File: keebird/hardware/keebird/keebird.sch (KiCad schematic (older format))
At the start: 9 parts

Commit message: Wire in 1.69 OLED display to the schematic.
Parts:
- added C?: 470uf, symbol Device:C_Small
- added J?: NHD_OLED_Display_Connector, symbol Connector:Conn_01x20_Male
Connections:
- net +3V3: now also C?.1, C?.2, J?.1 (Pin_1), J?.15 (Pin_15), J?.18 (Pin_18), J?.19 (Pin_19), J?.2 (Pin_2), J?.20 (Pin_20)
- net ADDR_0: now also J?.4 (Pin_4)
- net DATA_0: now also J?.7 (Pin_7)
- net DATA_1: now also J?.8 (Pin_8)
- net DATA_2: now also J?.9 (Pin_9)
- net DATA_3: now also J?.10 (Pin_10)
- net DATA_4: now also J?.11 (Pin_11)
- net DATA_5: now also J?.12 (Pin_12)
- net DATA_6: now also J?.13 (Pin_13)
- net DATA_7: now also J?.14 (Pin_14)
- net ~LCD_RST: now reaches U?.116 (PD2)
- net ~LCD_RST: now also J?.16 (Pin_16)
- net MEM_RD: now reaches U?.118 (PD4)
- net MEM_RD: now also J?.6 (Pin_6)
- net MEM_WR: now reaches U?.119 (PD5)
- net MEM_WR: now also J?.5 (Pin_5)
- net LCD_CS: now reaches U?.123 (PD7)
- net LCD_CS: now also J?.17 (Pin_17)
- no-connect marks 0 -> 1
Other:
- note added: "Place near LCD Power Pins"
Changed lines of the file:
@@
 LIBS:contrib
 LIBS:valves
+LIBS:keebird-cache
 EELAYER 26 0
 EELAYER END
@@
 Text Notes 9700 850  0    50   ~ 0
 Place Near RAM\n
+$Comp
+L Connector:Conn_01x20_Male J?
+U 1 1 5B82E830
+P 12050 6350
+F 0 "J?" H 12156 7428 50  0000 C CNN
+F 1 "NHD_OLED_Display_Connector" H 12156 7337 50  0000 C CNN
+F 2 "" H 12050 6350 50  0001 C CNN
+F 3 "~" H 12050 6350 50  0001 C CNN
+	1    12050 6350
+	1    0    0    -1
+$EndComp
+NoConn ~ 12250 5650
+Wire Wire Line
+	12250 6050 12450 6050
+Text Label 12450 6050 0    50   ~ 0
+DATA_0
+Wire Wire Line
+	12250 6150 12450 6150
+Text Label 12450 6150 0    50   ~ 0
+DATA_1
+Wire Wire Line
+	12250 6250 12450 6250
+Text Label 12450 6250 0    50   ~ 0
+DATA_2
+Wire Wire Line
+	12250 6350 12450 6350
+Text Label 12450 6350 0    50   ~ 0
+DATA_3
+Wire Wire Line
+	12250 6450 12450 6450
+Text Label 12450 6450 0    50   ~ 0
+DATA_4
+Wire Wire Line
+	12250 6550 12450 6550
+Text Label 12450 6550 0    50   ~ 0
+DATA_5
+Wire Wire Line
+	12250 6650 12450 6650
+Text Label 12450 6650 0    50   ~ 0
+DATA_6
+Wire Wire Line
+	12250 6750 12450 6750
+Text Label 12450 6750 0    50   ~ 0
+DATA_7
+Wire Wire Line
+	8250 7450 8500 7450
+Text Label 8500 7450 0    50   ~ 0
+LCD_CS
+Wire Wire Line
+	12250 7050 12450 7050
+Text Label 12450 7050 0    50   ~ 0
+LCD_CS
+Wire Wire Line
+	8250 7150 8500 7150
+Text Label 8500 7150 0    50   ~ 0
+MEM_RD
+Wire Wire Line
+	12250 5950 12450 5950
+Text Label 12450 5950 0    50   ~ 0
+MEM_RD
+Wire Wire Line
+	8250 7250 8500 7250
+Text Label 8500 7250 0    50   ~ 0
+MEM_WR
+Wire Wire Line
+	12250 5850 12450 5850
+Text Label 12450 5850 0    50   ~ 0
+MEM_WR
+Wire Wire Line
+	12250 5750 12450 5750
+Text Label 12450 5750 0    50   ~ 0
+ADDR_0
+Wire Wire Line
+	12250 6850 12450 6850
+$Comp
+L power:GND #PWR?
+U 1 1 5B8D1D5F
+P 12450 6850
+F 0 "#PWR?" H 12450 6600 50  0001 C CNN
+F 1 "GND" V 12455 6722 50  0000 R CNN
+F 2 "" H 12450 6850 50  0001 C CNN
+F 3 "" H 12450 6850 50  0001 C CNN
+	1    12450 6850
+	0    -1   -1   0
+$EndComp
+Wire Wire Line
+	12250 7150 12450 7150
+$Comp
+L power:GND #PWR?
+U 1 1 5B8DAB90
+P 12450 7150
+F 0 "#PWR?" H 12450 6900 50  0001 C CNN
+F 1 "GND" V 12455 7022 50  0000 R CNN
+F 2 "" H 12450 7150 50  0001 C CNN
+F 3 "" H 12450 7150 50  0001 C CNN
+	1    12450 7150
+	0    -1   -1   0
+$EndComp
+Wire Wire Line
+	12250 7350 12450 7350
+$Comp
+L power:GND #PWR?
+U 1 1 5B8E3ACA
+P 12450 7350
+F 0 "#PWR?" H 12450 7100 50  0001 C CNN
+F 1 "GND" V 12455 7222 50  0000 R CNN
+F 2 "" H 12450 7350 50  0001 C CNN
+F 3 "" H 12450 7350 50  0001 C CNN
+	1    12450 7350
+	0    -1   -1   0
+$EndComp
+Wire Wire Line
+	12250 5450 12450 5450
+$Comp
+L power:GND #PWR?
+U 1 1 5B8F5E9E
+P 12450 5450
+F 0 "#PWR?" H 12450 5200 50  0001 C CNN
+F 1 "GND" V 12455 5322 50  0000 R CNN
+F 2 "" H 12450 5450 50  0001 C CNN
+F 3 "" H 12450 5450 50  0001 C CNN
+	1    12450 5450
+	0    -1   -1   0
+$EndComp
+Wire Wire Line
+	12250 7250 12450 7250
+$Comp
+L power:+3.3V #PWR?
+U 1 1 5B90882C
+P 12450 7250
+F 0 "#PWR?" H 12450 7100 50  0001 C CNN
+F 1 "+3.3V" V 12465 7378 50  0000 L CNN
+F 2 "" H 12450 7250 50  0001 C CNN
+F 3 "" H 12450 7250 50  0001 C CNN
+	1    12450 7250
+	0    1    1    0
+$EndComp
+Wire Wire Line
+	12250 5550 12450 5550
+$Comp
+L power:+3.3V #PWR?
+U 1 1 5B91218E
+P 12450 5550
+F 0 "#PWR?" H 12450 5400 50  0001 C CNN
+F 1 "+3.3V" V 12465 5678 50  0000 L CNN
+F 2 "" H 12450 5550 50  0001 C CNN
+F 3 "" H 12450 5550 50  0001 C CNN
+	1    12450 5550
+	0    1    1    0
+$EndComp
+Wire Wire Line
+	12250 6950 12450 6950
+Text Label 12450 6950 0    50   ~ 0
+~LCD_RST
+Wire Wire Line
+	8250 6950 8500 6950
+Text Label 8500 6950 0    50   ~ 0
+~LCD_RST
+$Comp
+L Device:C_Small C?
+U 1 1 5B937C3F
+P 13600 5500
+F 0 "C?" H 13692 5546 50  0000 L CNN
+F 1 "470uf" H 13692 5455 50  0000 L CNN
+F 2 "" H 13600 5500 50  0001 C CNN
+F 3 "~" H 13600 5500 50  0001 C CNN
+	1    13600 5500
+	1    0    0    -1
+$EndComp
+Wire Wire Line
+	13600 5400 13600 5250
+$Comp
+L power:+3.3V #PWR?
+U 1 1 5B9407C0
+P 13600 5250
+F 0 "#PWR?" H 13600 5100 50  0001 C CNN
+F 1 "+3.3V" H 13615 5423 50  0000 C CNN
+F 2 "" H 13600 5250 50  0001 C CNN
+F 3 "" H 13600 5250 50  0001 C CNN
+	1    13600 5250
+	1    0    0    -1
+$EndComp
+Wire Wire Line
+	13600 5600 13600 5750
+$Comp
+L power:GND #PWR?
+U 1 1 5B949383
+P 13600 5750
+F 0 "#PWR?" H 13600 5500 50  0001 C CNN
+F 1 "GND" H 13605 5577 50  0000 C CNN
+F 2 "" H 13600 5750 50  0001 C CNN
+F 3 "" H 13600 5750 50  0001 C CNN
+	1    13600 5750
+	1    0    0    -1
+$EndComp
+Text Notes 14000 5500 0    50   ~ 0
+Place near LCD Power Pins
 $EndSCHEMATC

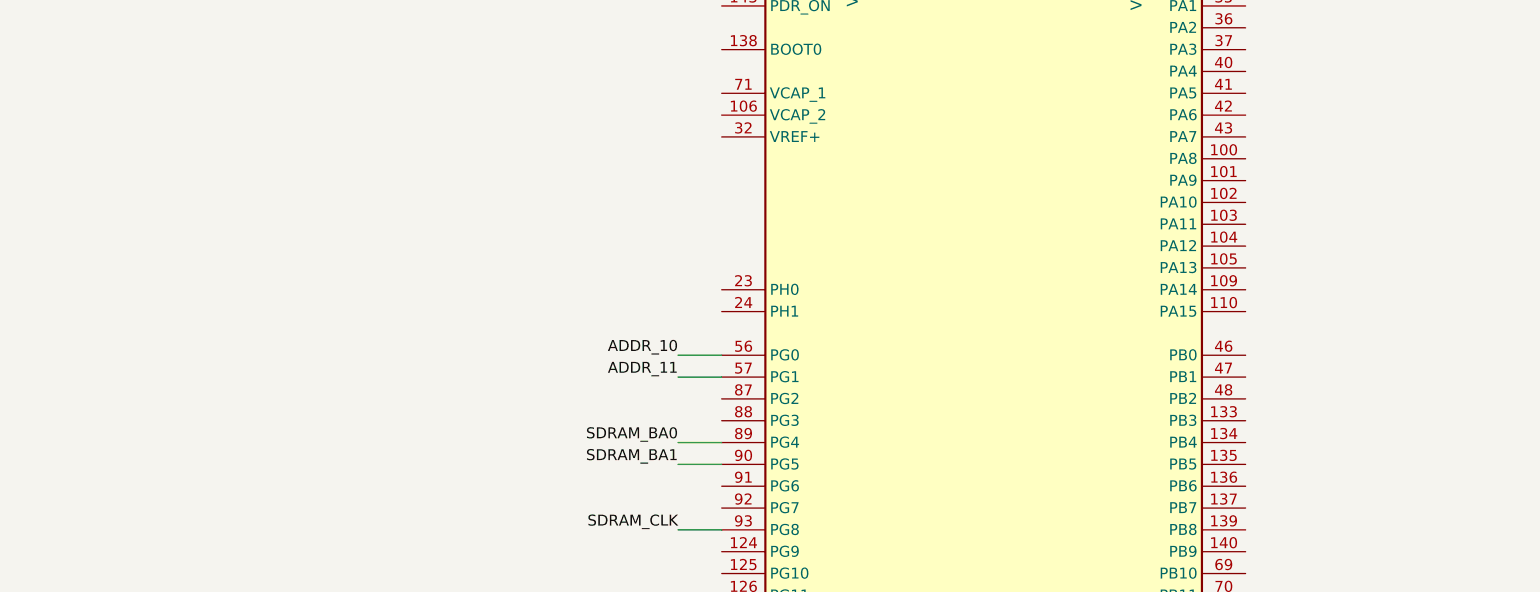
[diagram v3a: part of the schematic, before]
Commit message: Add USB connector
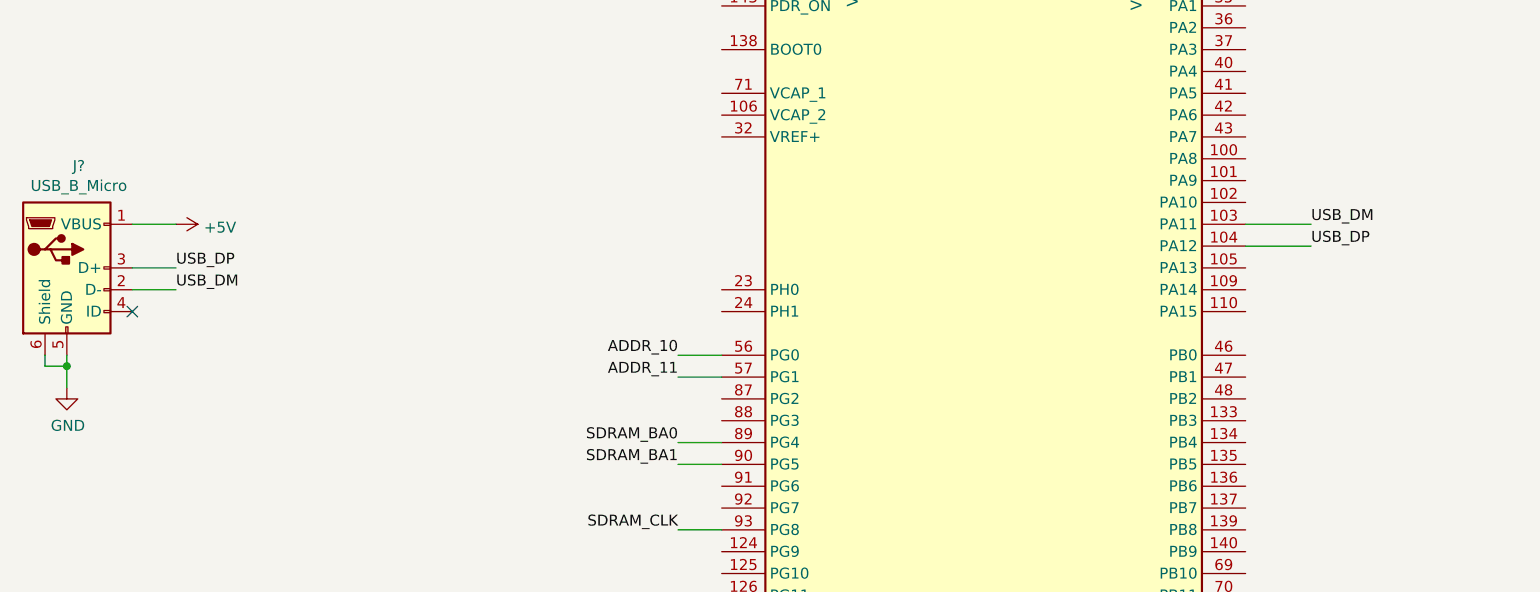
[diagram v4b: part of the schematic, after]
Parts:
- added J?: USB_B_Micro, symbol Connector:USB_B_Micro
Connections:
- net +3V3: now also J?.5 (GND), J?.6 (Shield)
- net USB_DM: now reaches U?.103 (PA11)
- net USB_DM: now also J?.2 (D-)
- net USB_DP: now reaches U?.104 (PA12)
- net USB_DP: now also J?.3 (D+)
- new net +5V: J?.1 (VBUS)
- no-connect marks 1 -> 2
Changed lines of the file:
@@
 Text Notes 14000 5500 0    50   ~ 0
 Place near LCD Power Pins
+Wire Wire Line
+	8250 2750 8550 2750
+Text Label 8550 2750 0    50   ~ 0
+USB_DM
+Wire Wire Line
+	8250 2850 8550 2850
+Text Label 8550 2850 0    50   ~ 0
+USB_DP
+Wire Wire Line
+	3150 2950 3350 2950
+Text Label 3350 2950 0    50   ~ 0
+USB_DP
+Wire Wire Line
+	3150 3050 3350 3050
+Text Label 3350 3050 0    50   ~ 0
+USB_DM
+NoConn ~ 3150 3150
+Wire Wire Line
+	2850 3350 2850 3400
+$Comp
+L power:GND #PWR?
+U 1 1 5B981332
+P 2850 3500
+F 0 "#PWR?" H 2850 3250 50  0001 C CNN
+F 1 "GND" H 2855 3327 50  0000 C CNN
+F 2 "" H 2850 3500 50  0001 C CNN
+F 3 "" H 2850 3500 50  0001 C CNN
+	1    2850 3500
+	1    0    0    -1
+$EndComp
+Wire Wire Line
+	3150 2750 3350 2750
+$Comp
+L power:+5V #PWR?
+U 1 1 5B9C3EC4
+P 3350 2750
+F 0 "#PWR?" H 3350 2600 50  0001 C CNN
+F 1 "+5V" V 3365 2878 50  0000 L CNN
+F 2 "" H 3350 2750 50  0001 C CNN
+F 3 "" H 3350 2750 50  0001 C CNN
+	1    3350 2750
+	0    1    1    0
+$EndComp
+$Comp
+L Connector:USB_B_Micro J?
+U 1 1 5B9C425C
+P 2850 2950
+F 0 "J?" H 2905 3417 50  0000 C CNN
+F 1 "USB_B_Micro" H 2905 3326 50  0000 C CNN
+F 2 "" H 3000 2900 50  0001 C CNN
+F 3 "~" H 3000 2900 50  0001 C CNN
+	1    2850 2950
+	1    0    0    -1
+$EndComp
+Wire Wire Line
+	2750 3350 2750 3400
+Wire Wire Line
+	2750 3400 2850 3400
+Connection ~ 2850 3400
+Wire Wire Line
+	2850 3400 2850 3500
 $EndSCHEMATC

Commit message: Add 8MHZ crystal oscillator.
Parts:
- added C? (x2): 24pF, symbol Device:C_Small
- added Y?: 8MHZ, symbol Device:Crystal_Small
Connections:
- net +3V3: now also C?.1, C?.2
- net at U?.23 (PH0): now also C?.1, Y?.1
- net at U?.24 (PH1): now also C?.2, Y?.2
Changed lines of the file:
@@
 Wire Wire Line
 	2850 3400 2850 3500
+$Comp
+L Device:Crystal_Small Y?
+U 1 1 5B87EB8B
+P 5150 3100
+F 0 "Y?" V 5104 3188 50  0000 L CNN
+F 1 "8MHZ" V 5195 3188 50  0000 L CNN
+F 2 "" H 5150 3100 50  0001 C CNN
+F 3 "~" H 5150 3100 50  0001 C CNN
+	1    5150 3100
+	0    1    1    0
+$EndComp
+$Comp
+L Device:C_Small C?
+U 1 1 5B87ECB0
+P 4900 3000
+F 0 "C?" V 4671 3000 50  0000 C CNN
+F 1 "24pF" V 4762 3000 50  0000 C CNN
+F 2 "" H 4900 3000 50  0001 C CNN
+F 3 "~" H 4900 3000 50  0001 C CNN
+	1    4900 3000
+	0    1    1    0
+$EndComp
+$Comp
+L Device:C_Small C?
+U 1 1 5B87EDA3
+P 4900 3200
+F 0 "C?" V 4671 3200 50  0000 C CNN
+F 1 "24pF" V 4762 3200 50  0000 C CNN
+F 2 "" H 4900 3200 50  0001 C CNN
+F 3 "~" H 4900 3200 50  0001 C CNN
+	1    4900 3200
+	0    -1   -1   0
+$EndComp
+Wire Wire Line
+	5850 3050 5550 3050
+Wire Wire Line
+	5550 3050 5550 3000
+Wire Wire Line
+	5550 3000 5150 3000
+Wire Wire Line
+	5150 3200 5550 3200
+Wire Wire Line
+	5550 3200 5550 3150
+Wire Wire Line
+	5550 3150 5850 3150
+Wire Wire Line
+	5150 3000 5000 3000
+Connection ~ 5150 3000
+Wire Wire Line
+	4800 3000 4650 3000
+Wire Wire Line
+	4650 3000 4650 3100
+Wire Wire Line
+	4650 3200 4800 3200
+Wire Wire Line
+	5000 3200 5150 3200
+Connection ~ 5150 3200
+Wire Wire Line
+	4650 3100 4450 3100
+Wire Wire Line
+	4450 3100 4450 3150
+Connection ~ 4650 3100
+Wire Wire Line
+	4650 3100 4650 3200
+$Comp
+L power:GND #PWR?
+U 1 1 5B8EF0DC
+P 4450 3150
+F 0 "#PWR?" H 4450 2900 50  0001 C CNN
+F 1 "GND" H 4455 2977 50  0000 C CNN
+F 2 "" H 4450 3150 50  0001 C CNN
+F 3 "" H 4450 3150 50  0001 C CNN
+	1    4450 3150
+	1    0    0    -1
+$EndComp
 $EndSCHEMATC

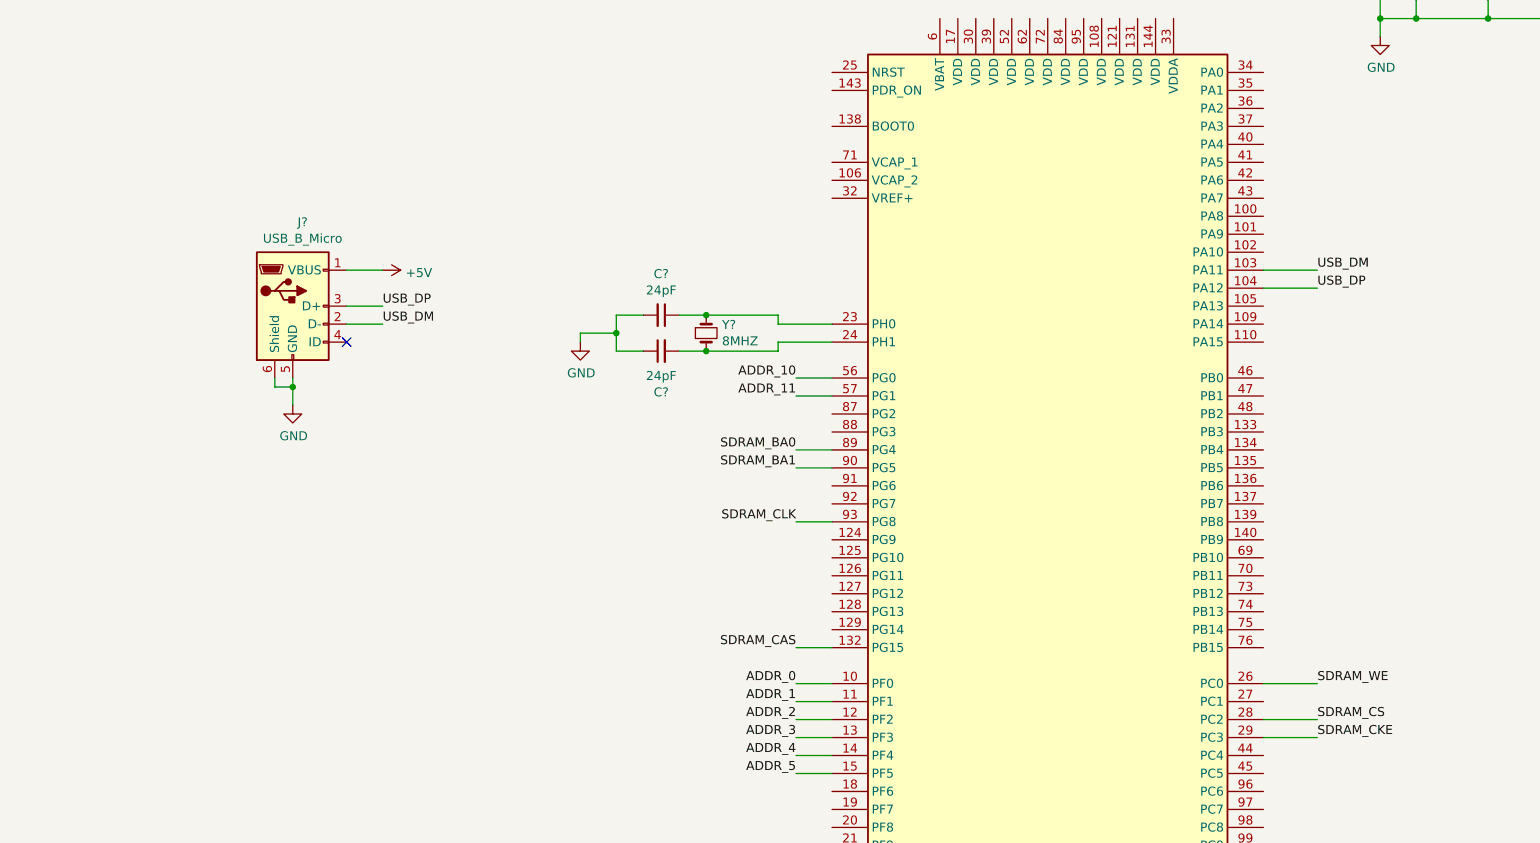
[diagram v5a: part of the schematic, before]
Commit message: Wire in flash serial IC.
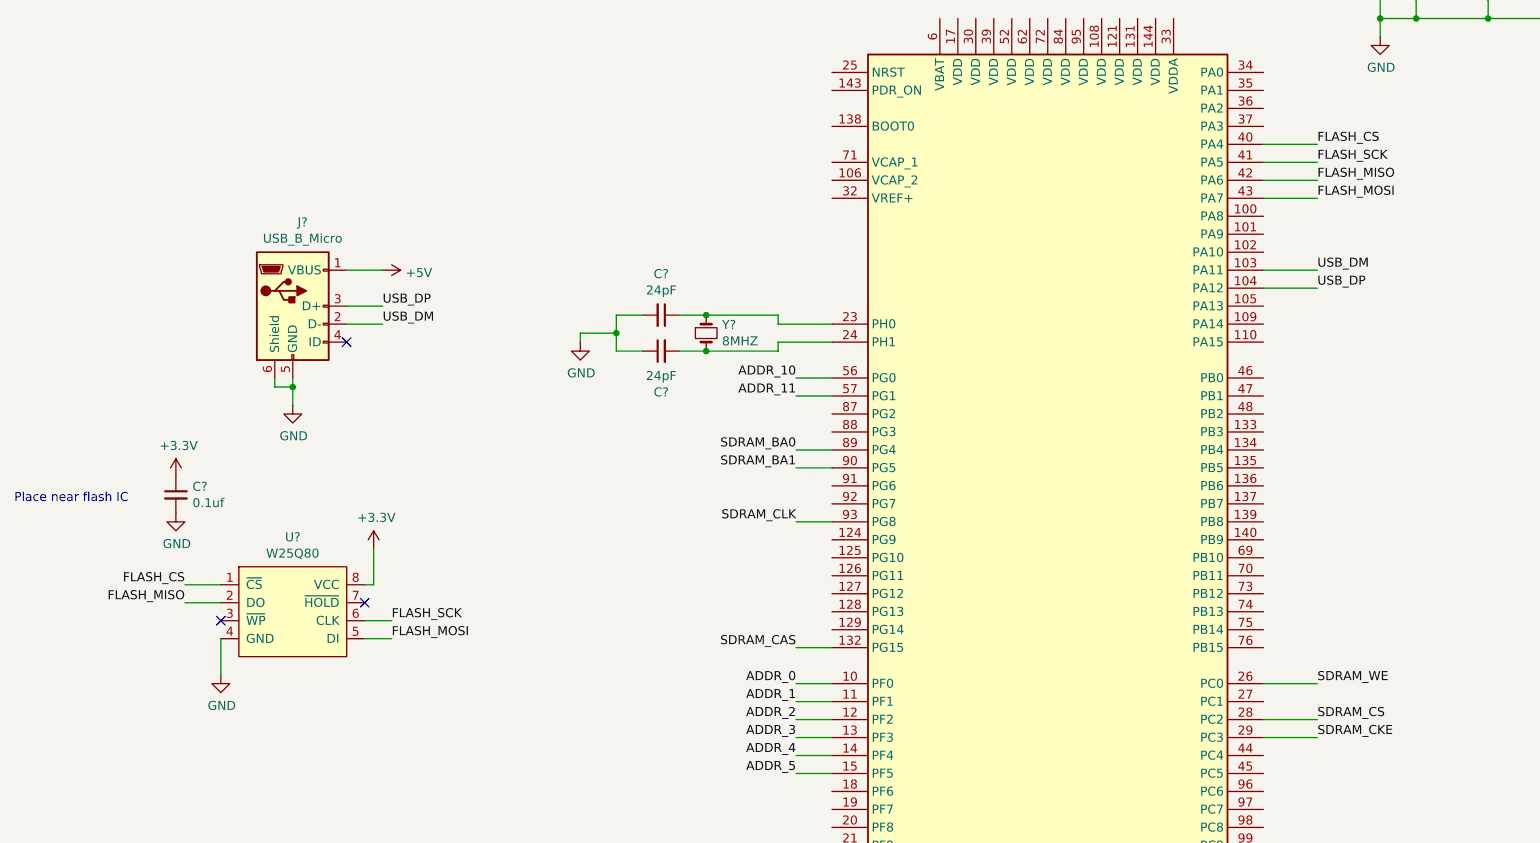
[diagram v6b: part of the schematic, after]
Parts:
- added C?: 0.1uf, symbol Device:C_Small
- added U?: W25Q80, symbol custom_ic:W25Q80
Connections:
- net +3V3: now also C?.1, C?.2, U?.4 (GND), U?.8 (VCC)
- net FLASH_CS: now reaches U?.40 (PA4)
- net FLASH_CS: now also U?.1 (~CS)
- net FLASH_SCK: now reaches U?.41 (PA5)
- net FLASH_SCK: now also U?.6 (CLK)
- net FLASH_MISO: now reaches U?.42 (PA6)
- net FLASH_MISO: now also U?.2 (DO)
- net FLASH_MOSI: now reaches U?.43 (PA7)
- net FLASH_MOSI: now also U?.5 (DI)
- no-connect marks 2 -> 4
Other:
- note added: "Place near flash IC"
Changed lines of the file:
@@
 	1    0    0    -1
 $EndComp
+$Comp
+L custom_ic:W25Q80 U?
+U 1 1 5B908227
+P 2850 4650
+F 0 "U?" H 2850 5065 50  0000 C CNN
+F 1 "W25Q80" H 2850 4974 50  0000 C CNN
+F 2 "" H 2850 4550 50  0001 C CNN
+F 3 "" H 2850 4550 50  0001 C CNN
+	1    2850 4650
+	1    0    0    -1
+$EndComp
+Wire Wire Line
+	3250 4500 3300 4500
+Wire Wire Line
+	3300 4500 3300 4300
+$Comp
+L power:+3.3V #PWR?
+U 1 1 5B91472E
+P 3300 4300
+F 0 "#PWR?" H 3300 4150 50  0001 C CNN
+F 1 "+3.3V" H 3315 4473 50  0000 C CNN
+F 2 "" H 3300 4300 50  0001 C CNN
+F 3 "" H 3300 4300 50  0001 C CNN
+	1    3300 4300
+	1    0    0    -1
+$EndComp
+Wire Wire Line
+	2450 4800 2450 5000
+$Comp
+L power:GND #PWR?
+U 1 1 5B920C57
+P 2450 5000
+F 0 "#PWR?" H 2450 4750 50  0001 C CNN
+F 1 "GND" H 2455 4827 50  0000 C CNN
+F 2 "" H 2450 5000 50  0001 C CNN
+F 3 "" H 2450 5000 50  0001 C CNN
+	1    2450 5000
+	1    0    0    -1
+$EndComp
+Wire Wire Line
+	8250 2150 8550 2150
+Text Label 8550 2150 0    50   ~ 0
+FLASH_SCK
+Wire Wire Line
+	3250 4700 3400 4700
+Text Label 3400 4700 0    50   ~ 0
+FLASH_SCK
+Wire Wire Line
+	3250 4800 3400 4800
+Text Label 3400 4800 0    50   ~ 0
+FLASH_MOSI
+Wire Wire Line
+	2450 4600 2250 4600
+Text Label 2250 4600 2    50   ~ 0
+FLASH_MISO
+Wire Wire Line
+	2450 4500 2250 4500
+Text Label 2250 4500 2    50   ~ 0
+FLASH_CS
+NoConn ~ 2450 4700
+NoConn ~ 3250 4600
+Wire Wire Line
+	8250 2050 8550 2050
+Text Label 8550 2050 0    50   ~ 0
+FLASH_CS
+Wire Wire Line
+	8250 2250 8550 2250
+Text Label 8550 2250 0    50   ~ 0
+FLASH_MISO
+Wire Wire Line
+	8250 2350 8550 2350
+Text Label 8550 2350 0    50   ~ 0
+FLASH_MOSI
+$Comp
+L Device:C_Small C?
+U 1 1 5B9B3158
+P 2200 4000
+F 0 "C?" H 2292 4046 50  0000 L CNN
+F 1 "0.1uf" H 2292 3955 50  0000 L CNN
+F 2 "" H 2200 4000 50  0001 C CNN
+F 3 "~" H 2200 4000 50  0001 C CNN
+	1    2200 4000
+	1    0    0    -1
+$EndComp
+$Comp
+L power:+3.3V #PWR?
+U 1 1 5B9B3204
+P 2200 3900
+F 0 "#PWR?" H 2200 3750 50  0001 C CNN
+F 1 "+3.3V" H 2215 4073 50  0000 C CNN
+F 2 "" H 2200 3900 50  0001 C CNN
+F 3 "" H 2200 3900 50  0001 C CNN
+	1    2200 3900
+	1    0    0    -1
+$EndComp
+$Comp
+L power:GND #PWR?
+U 1 1 5B9B3298
+P 2200 4100
+F 0 "#PWR?" H 2200 3850 50  0001 C CNN
+F 1 "GND" H 2205 3927 50  0000 C CNN
+F 2 "" H 2200 4100 50  0001 C CNN
+F 3 "" H 2200 4100 50  0001 C CNN
+	1    2200 4100
+	1    0    0    -1
+$EndComp
+Text Notes 1300 4050 0    50   ~ 0
+Place near flash IC
 $EndSCHEMATC
